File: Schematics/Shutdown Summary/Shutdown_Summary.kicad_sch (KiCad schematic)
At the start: 48 parts, among them J1 GND, J2 TS+, J3 TS-, J4 Main TS Connector, K1 Omron DPDT Relay, K10 SPST-NO (Precharge), K11 SPST-NO (AIR), K12 SPST-NO (AIR), K2 Omron DPDT Relay, K3 Omron DPDT Relay, K4 Omron DPDT Relay, K5 Omron DPDT Relay, K6 Omron DPDT Relay, K7 SPST-NO (Precharge Control), K8 SPST-NO (AIR Control), K9 SPST-NC (Discharge), SW1 GLVMS, SW10 SMD/HVD 1, SW2 Side BRB, SW3 Side BRB, SW4 Brake Over-Travel Switch, SW5 Latching Circuit Reset, SW6 Cockpit BRB, SW7 TSMS, SW8 SMD/HVD 3, SW9 SMD/HVD 2, U1 FuseBox_PSZACCEPS052H, U2 Bender_Isometer_IR155-3204

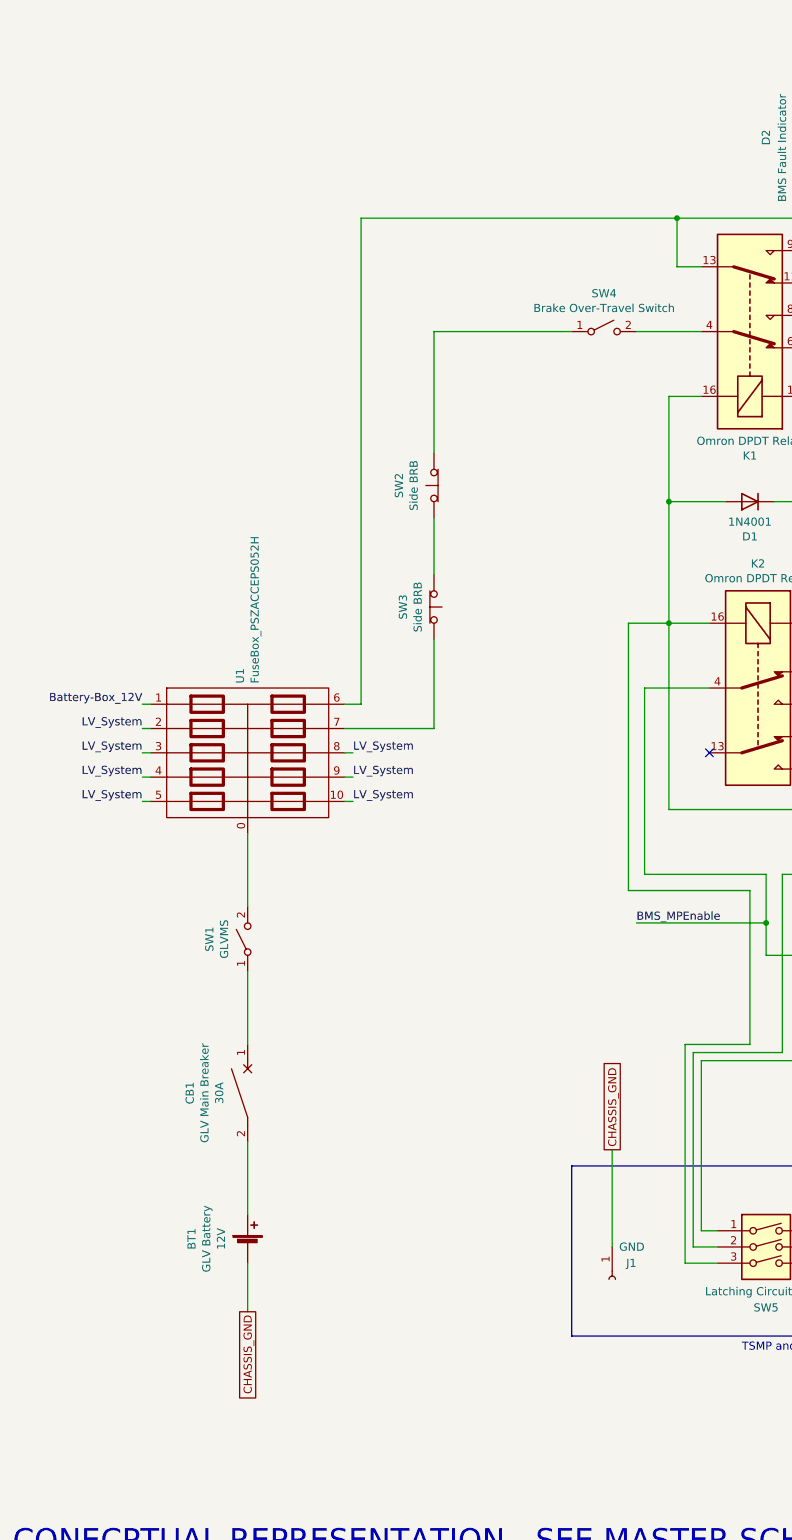
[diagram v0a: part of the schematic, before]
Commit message: Moved BRB in shutdown summary
Same change, but in shutdown summary schematic
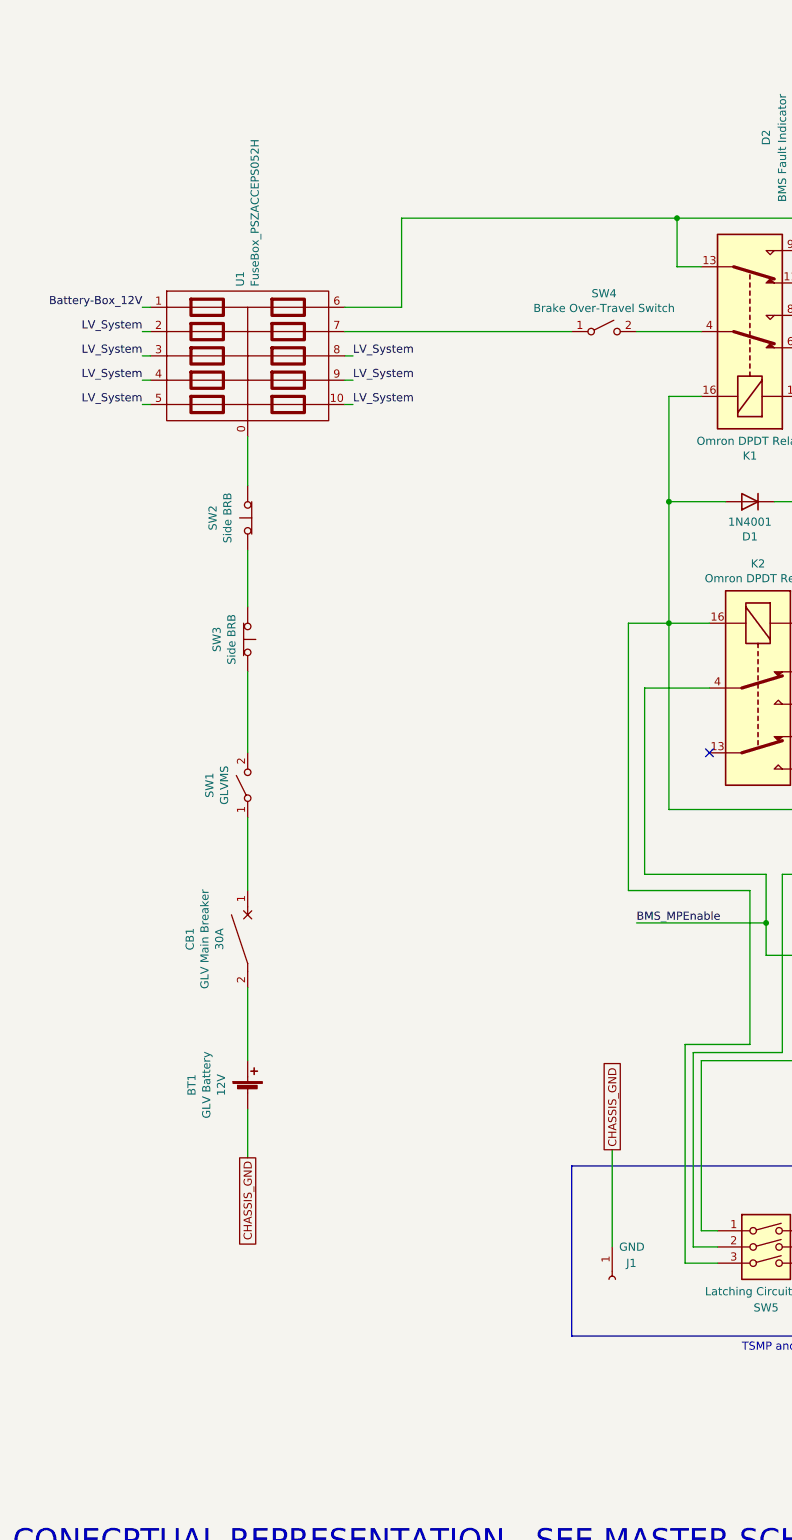
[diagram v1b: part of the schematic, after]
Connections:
- net at SW1.2 (B): now also SW3.2 (B); no longer U1.0
- net at U1.7: now also SW4.1 (A); no longer SW3.2 (B)
- net at SW2.2 (B): now also U1.0; no longer SW4.1 (A)
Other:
- moved on the sheet: BT1, CB1, SW1, SW2, SW3, U1

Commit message: Esf1 updates (#135)
* OPened schmetic

* Renamed SMD/HVDs

* Made CAN non-latching

* Removed SSOKs

* Reformating

* Cleanup

* Export
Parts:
- removed D7, D8: SSOK, symbol Device:LED
- removed K6: Omron DPDT Relay, Relay_THT:Relay_DPDT_Omron_G5V-2, symbol Relay:G5V-2
- SW10: value SMD/HVD 1 -> SMD 1
- SW8: value SMD/HVD 3 -> SMD 2
- SW9: value SMD/HVD 2 -> HVD
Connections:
- net BMS_MPEnable: now also D5.1 (K), K5.16
- now unconnected: SW5.1
- no-connect marks 17 -> 13
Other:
- moved on the sheet: D3, D4, D5, D6, K3, K4, K5, SW6, SW7, U2

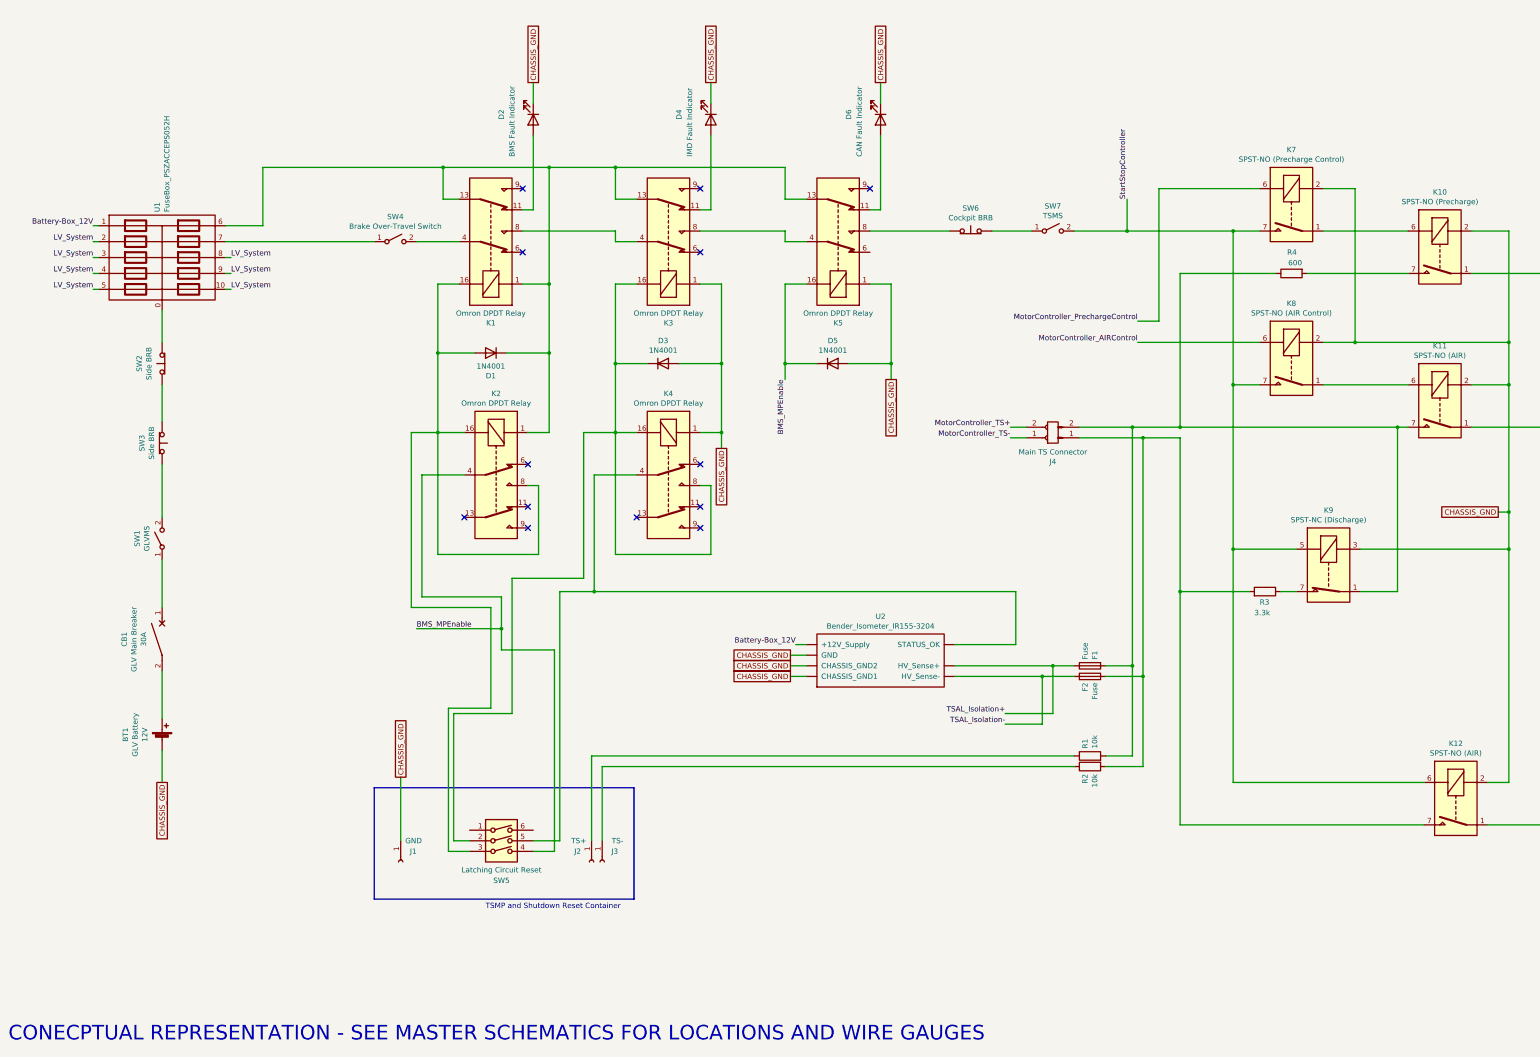
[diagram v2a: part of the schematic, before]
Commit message: ESF-2 2023 Updates (#136)
* Moved shutdown loop & TSMPs

* Moved Dashboard/Footwellbox

* Deleted SSOKs

* More stuff

* Charger and battbox stuff

* Added battbox fans

* Updated sheet sizing

* Flipped MC

 to make powertrain ordering better

* Updated HV plate

* IDrk

* Better topsheet labels

* Segment Layer updates

Adding shepherd

* LV Plate update

* Partial work on accumulator container sheet

To be continued

* Finish accumulator

* Footwell updates

* Removing old files

* Added Wheel

* Top sheet budge

* Renumbered pages

* Shutdown Summary Updates

* Missed some TSV color

* Export shutdown summary

* Deleted more old files

* Added TSAL17

* Added TS-GLV17

* Added Wheel17

* Other NER lib cleanup

* Annotations

* More annotate and export

* Moved PDF

* Reexport master schem

* Cleaning out old shutdown summary files

* MATLAB!

For precharge and discharge plotting

* Changed label alignment

* Updated dashboard name

* Updated for LFP board and bigger top sheet

* backup

* Changed breaker to fuse in Shutdown Simmary

* Finished traces

* Oops forgot to merge
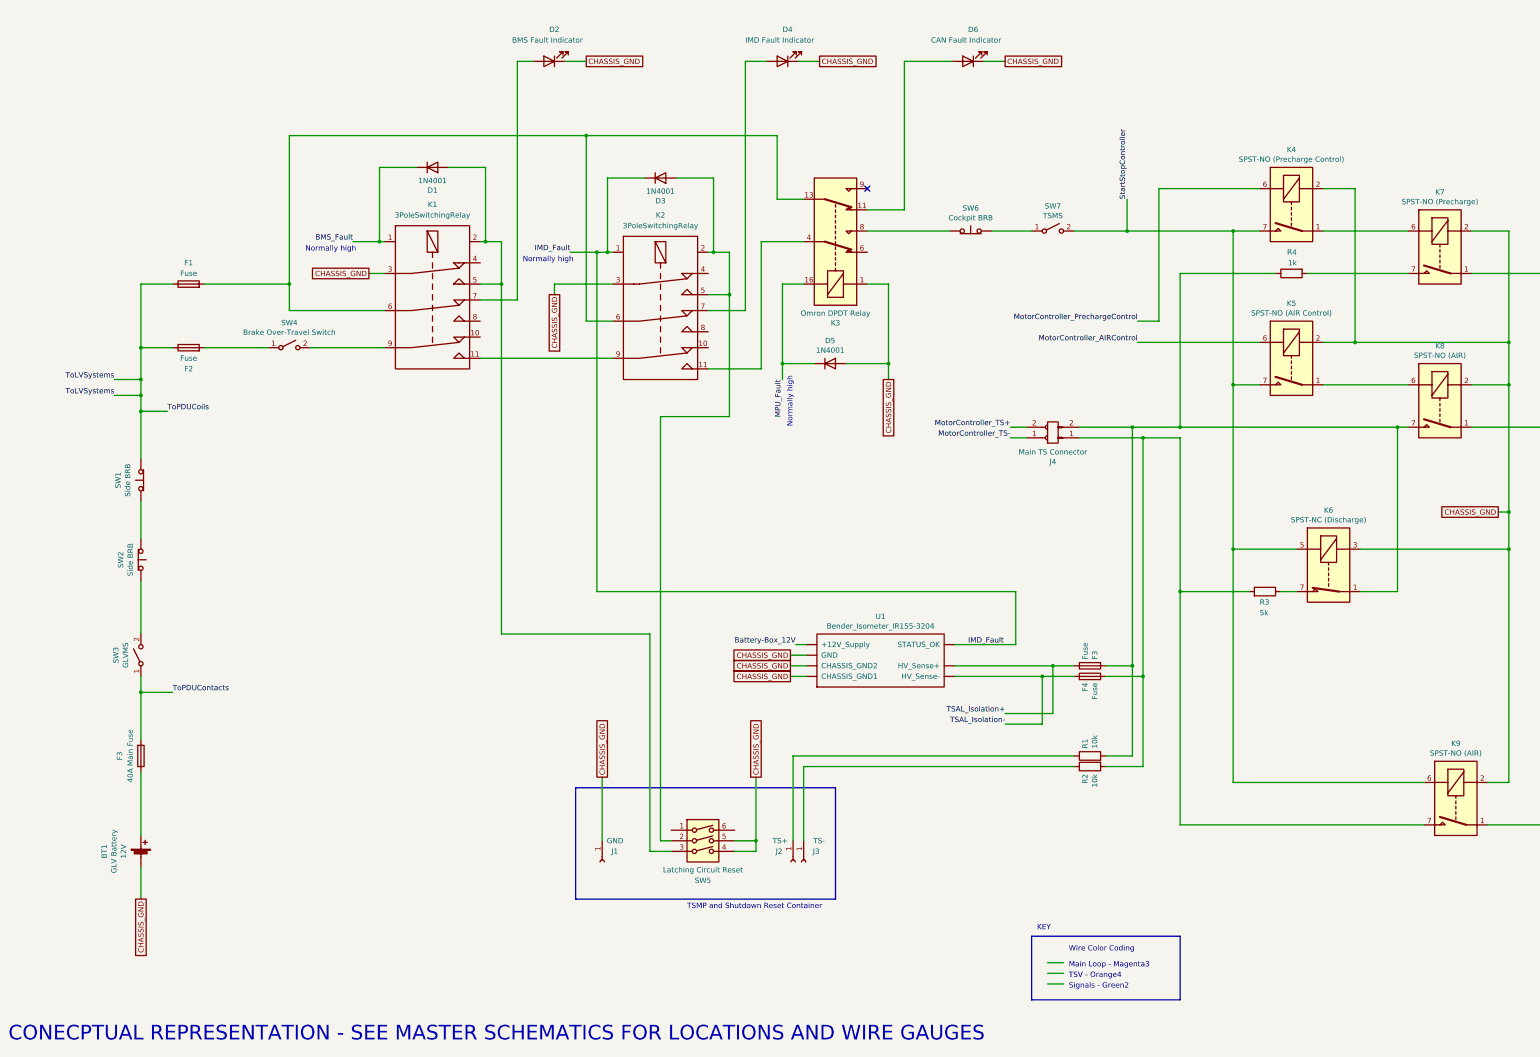
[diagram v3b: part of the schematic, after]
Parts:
- removed CB1: GLV Main Breaker, symbol Device:CircuitBreaker_1P
- removed K1, K2, K3, K4: Omron DPDT Relay, Relay_THT:Relay_DPDT_Omron_G5V-2, symbol Relay:G5V-2
- removed U1: FuseBox_PSZACCEPS052H, symbol NER:FuseBox_PSZACCEPS052H
- added F1, F2: Fuse, symbol Device:Fuse
- added F3: 40A Main Fuse, symbol Device:Fuse
- added K1, K2: 3PoleSwitchingRelay, symbol NER:3PoleSwitchingRelay
- R3: value 3.3k -> 5k
- R4: value 600 -> 1k
- renumbered F1 to F3, F2 to F4, K5 to K3, K7 to K4, K8 to K5, K9 to K6, K10 to K7, K11 to K8, K12 to K9, SW2 to SW1, SW3 to SW2, SW1 to SW3, U2 to U1
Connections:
- net CHASSIS_GND: now also SW5.4, SW5.5, K1.3, K2.3; no longer D3.2 (A)
- net at BT1.1 (+): now also F3.1
- net ToPDUContacts: now reaches SW3.1 (A)
- net ToPDUContacts: now also F3.2
- net ToLVSystems: now reaches SW1.2 (B)
- net ToLVSystems: now also F1.1, F2.1
- net at SW4.1 (A): now also F2.2
- net at SW4.2 (B): now also K1.9
- net at K3.13: now also F1.2, K1.6, K2.6; no longer D1.1 (K)
- net at SW5.2: now also D3.2 (A), K2.2, K2.5; no longer D3.1 (K)
- net at D4.2 (A): now also K2.7
- net at K3.4: now also K2.11
- net at D1.2 (A), SW5.3: now also K1.2, K1.5
- net at D2.2 (A): now also K1.7
- net BMS_MPEnable renamed MPU_Fault
- net MPU_Fault: no longer SW5.4
- new net: K1.11, K2.9
- new net BMS_Fault: D1.1 (K), K1.1
- new net IMD_Fault: D3.1 (K), K2.1, U1.~ (STATUS_OK)
- no-connect marks 13 -> 1
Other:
- note added: "KEY"
- note added: "Main Loop - Magenta3"
- note added: "Normally high"
- note added: "Signals - Green2"
- note added: "TSV - Orange4"
- note added: "Wire Color Coding"
- moved on the sheet: BT1, D2, D5, D6, J1, J2, J3, K3, SW1, SW2, SW3, SW4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

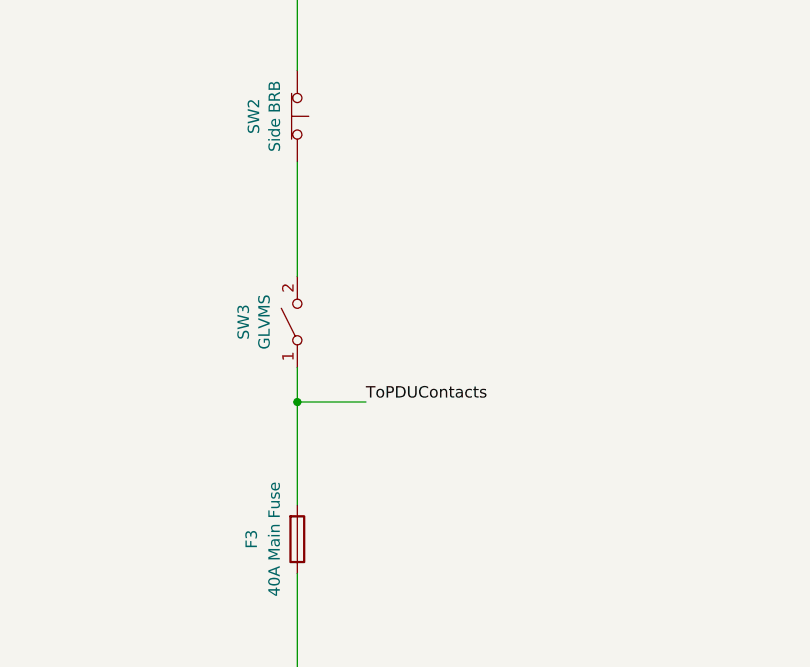
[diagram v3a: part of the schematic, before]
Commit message: Updated shutdown for ESF
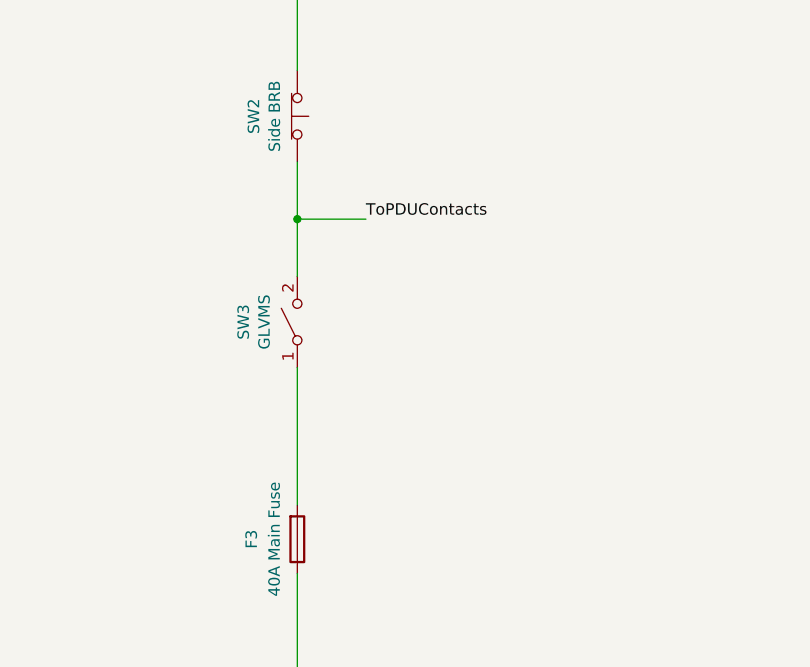
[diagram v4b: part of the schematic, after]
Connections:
- net ToPDUContacts: now also SW2.2 (B), SW3.2 (B); no longer F3.2, SW3.1 (A)
- new net: F3.2, SW3.1 (A)
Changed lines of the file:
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@@
   (title_block
     (title "Shutdown Circuit Summary")
-    (date "2023-02-02")
-    (rev "5")
+    (date "2023-03-19")
+    (rev "6")
     (company "Northeastern Electric Racing")
     (comment 1 "https://github.com/Northeastern-Electric-Racing/NER")
@@
   (junction (at 264.16 176.53) (diameter 0) (color 0 0 0 0)
   )
+  (junction (at 48.26 160.02) (diameter 0) (color 0 0 0 0)
+  )
   (junction (at 375.92 146.05) (diameter 0) (color 0 0 0 0)
-  )
-  (junction (at 48.26 180.34) (diameter 0) (color 0 0 0 0)
   )
   (junction (at 349.25 116.84) (diameter 0) (color 0 0 0 0)
@@
     (stroke (width 0.4) (type default) (color 255 153 0 1))
   )
-  (wire (pts (xy 48.26 180.34) (xy 48.26 176.53))
+  (wire (pts (xy 48.26 176.53) (xy 48.26 191.77))
     (stroke (width 0.5) (type default) (color 255 0 255 1))
   )
@@
   )
   (wire (pts (xy 48.26 105.41) (xy 48.26 109.22))
+    (stroke (width 0.5) (type default) (color 255 0 255 1))
+  )
+  (wire (pts (xy 48.26 160.02) (xy 48.26 166.37))
     (stroke (width 0.5) (type default) (color 255 0 255 1))
   )
@@
     (stroke (width 0) (type default) (color 0 0 0 0))
   )
+  (wire (pts (xy 48.26 160.02) (xy 55.88 160.02))
+    (stroke (width 0) (type default) (color 0 0 0 0))
+  )
   (wire (pts (xy 157.48 74.93) (xy 157.48 156.21))
     (stroke (width 0) (type default) (color 0 0 0 0))
@@
     (stroke (width 0.4) (type default) (color 255 153 0 1))
   )
-  (wire (pts (xy 48.26 180.34) (xy 48.26 191.77))
-    (stroke (width 0.5) (type default) (color 255 0 255 1))
-  )
   (polyline (pts (xy 297.18 238.76) (xy 261.62 238.76))
     (stroke (width 0) (type default) (color 0 0 0 0))
@@
     (stroke (width 0) (type default) (color 0 0 0 0))
   )
-  (wire (pts (xy 48.26 180.34) (xy 55.88 180.34))
-    (stroke (width 0) (type default) (color 0 0 0 0))
-  )
   (wire (pts (xy 243.205 173.99) (xy 266.7 173.99))
     (stroke (width 0.4) (type default) (color 255 153 0 1))
@@
     (stroke (width 0) (type default) (color 0 0 0 0))
   )
-  (wire (pts (xy 48.26 153.67) (xy 48.26 166.37))
+  (wire (pts (xy 48.26 153.67) (xy 48.26 160.02))
     (stroke (width 0.5) (type default) (color 255 0 255 1))
   )
@@
     (effects (font (size 1.27 1.27)) (justify right bottom))
   )
-  (label "ToPDUContacts" (at 55.88 180.34 0)
-    (effects (font (size 1.27 1.27)) (justify left bottom))
-  )
   (label "IMD_Fault" (at 151.13 74.93 180)
     (effects (font (size 1.27 1.27)) (justify right bottom))
@@
     (effects (font (size 1.27 1.27)) (justify right bottom))
   )
+  (label "ToPDUContacts" (at 55.88 160.02 0)
+    (effects (font (size 1.27 1.27)) (justify left bottom))
+  )
   (label "Battery-Box_12V" (at 205.105 168.91 180)

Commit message: Updated shutdown summary and exported
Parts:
- added F4: 40A, symbol Device:Fuse
- added F5, F6, F7: 15A, symbol Device:Fuse
- added F8, F9: 5A, symbol Device:Fuse
- added SW3A2: GLVMS, symbol Switch:SW_SPST
- added U2: TS-GLV17, symbol NER:TS-GLV17
- F10: renamed from F3; value Fuse -> 0.5A
- F11: renamed from F4; value Fuse -> 0.5A
- R3: value 5k -> 2.35k
- renumbered F3 to F1, F1 to F2, F2 to F3, SW4 to SW3, SW3 to SW3A1, SW5 to SW4, SW6 to SW5, SW7 to SW6, SW8 to SW7, SW9 to SW8, SW10 to SW9
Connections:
- net CHASSIS_GND: now also U2.1 (TS+), U2.2 (TS-), U2.3 (VoltMeas)
- net at F1.2, SW3A1.1 (A): now also SW3A2.2 (B)
- net at F10.2, J4.2, K6.1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: now also F8.2
- net at F11.1, J4.1, K9.7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: now also F9.1
- new net: F4.2, F5.1, F6.1, F7.1
- new net: F5.2, U2.6 (13V)
- new net: F9.2, U2.2 (TS-)
- new net: F6.2, U2.5 (13V)
- new net: F4.1, SW3A2.1 (A)
- new net: F8.1, U2.1 (TS+)
- new net: F7.2, U2.4 (PGOOD)
- new net ToTelemetry: U2.1 (TS+), U2.2 (TS-), U2.3 (VoltMeas), U2.4 (PGOOD)
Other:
- moved on the sheet: F10, F11, J1, J2, J3, R1, R2, SW4, U1
